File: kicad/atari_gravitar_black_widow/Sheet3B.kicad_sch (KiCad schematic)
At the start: 106 parts, among them Q1 2N3904, Y1 12.096 MHZ

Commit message: C16-30
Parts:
- C18, C19, C20, C21, C22, C25, C26, C37, C40, C41, C42, C43, C45, C46, C47, C48, C49, C50, C51, C52, C53, C54, C55, C56, C57, C58, C59, C60, C61, C62, C63: footprint (none) -> Star_Wars_Vector_PCB:GenericComp
- C23, C24: footprint (none) -> Star_Wars_Vector_PCB:CapBrown
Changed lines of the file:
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@@
       (effects (font (size 1.27 1.27)) (justify left))
     )
-    (property "Footprint" "" (id 2) (at 147.0152 207.01 0)
+    (property "Footprint" "Star_Wars_Vector_PCB:GenericComp" (id 2) (at 147.0152 207.01 0)
       (effects (font (size 1.27 1.27)) hide)
     )
@@
       (effects (font (size 1.27 1.27)) (justify left))
     )
-    (property "Footprint" "" (id 2) (at 108.9152 223.52 0)
+    (property "Footprint" "Star_Wars_Vector_PCB:GenericComp" (id 2) (at 108.9152 223.52 0)
       (effects (font (size 1.27 1.27)) hide)
     )
@@
       (effects (font (size 1.27 1.27)) (justify left))
     )
-    (property "Footprint" "" (id 2) (at 118.4402 223.52 0)
+    (property "Footprint" "Star_Wars_Vector_PCB:GenericComp" (id 2) (at 118.4402 223.52 0)
       (effects (font (size 1.27 1.27)) hide)
     )
@@
       (effects (font (size 1.27 1.27)) (justify left))
     )
-    (property "Footprint" "" (id 2) (at 127.9652 223.52 0)
+    (property "Footprint" "Star_Wars_Vector_PCB:GenericComp" (id 2) (at 127.9652 223.52 0)
       (effects (font (size 1.27 1.27)) hide)
     )
@@
       (effects (font (size 1.27 1.27)) (justify left))
     )
-    (property "Footprint" "" (id 2) (at 137.4902 223.52 0)
+    (property "Footprint" "Star_Wars_Vector_PCB:GenericComp" (id 2) (at 137.4902 223.52 0)
       (effects (font (size 1.27 1.27)) hide)
     )
@@
       (effects (font (size 1.27 1.27)) (justify left))
     )
-    (property "Footprint" "" (id 2) (at 147.0152 223.52 0)
+    (property "Footprint" "Star_Wars_Vector_PCB:GenericComp" (id 2) (at 147.0152 223.52 0)
       (effects (font (size 1.27 1.27)) hide)
     )
@@
       (effects (font (size 1.27 1.27)) (justify left))
     )
-    (property "Footprint" "" (id 2) (at 73.3552 242.57 0)
+    (property "Footprint" "Star_Wars_Vector_PCB:GenericComp" (id 2) (at 73.3552 242.57 0)
       (effects (font (size 1.27 1.27)) hide)
     )
@@
       (effects (font (size 1.27 1.27)) (justify left))
     )
-    (property "Footprint" "" (id 2) (at 82.8802 242.57 0)
+    (property "Footprint" "Star_Wars_Vector_PCB:GenericComp" (id 2) (at 82.8802 242.57 0)
       (effects (font (size 1.27 1.27)) hide)
     )
@@
       (effects (font (size 1.27 1.27)) (justify left))
     )
-    (property "Footprint" "" (id 2) (at 92.4052 242.57 0)
+    (property "Footprint" "Star_Wars_Vector_PCB:GenericComp" (id 2) (at 92.4052 242.57 0)
       (effects (font (size 1.27 1.27)) hide)
     )
@@
       (effects (font (size 1.27 1.27)) (justify left))
     )
-    (property "Footprint" "" (id 2) (at 101.9302 242.57 0)
+    (property "Footprint" "Star_Wars_Vector_PCB:GenericComp" (id 2) (at 101.9302 242.57 0)
       (effects (font (size 1.27 1.27)) hide)
     )
@@
       (effects (font (size 1.27 1.27)) (justify left))
     )
-    (property "Footprint" "" (id 2) (at 111.4552 242.57 0)
+    (property "Footprint" "Star_Wars_Vector_PCB:GenericComp" (id 2) (at 111.4552 242.57 0)
       (effects (font (size 1.27 1.27)) hide)
     )
@@
       (effects (font (size 1.27 1.27)) (justify left))
     )
-    (property "Footprint" "" (id 2) (at 120.9802 242.57 0)
+    (property "Footprint" "Star_Wars_Vector_PCB:GenericComp" (id 2) (at 120.9802 242.57 0)
       (effects (font (size 1.27 1.27)) hide)
     )
@@
       (effects (font (size 1.27 1.27)) (justify left))
     )
-    (property "Footprint" "" (id 2) (at 130.5052 242.57 0)
+    (property "Footprint" "Star_Wars_Vector_PCB:GenericComp" (id 2) (at 130.5052 242.57 0)
       (effects (font (size 1.27 1.27)) hide)
     )
@@
       (effects (font (size 1.27 1.27)) (justify left))
     )
-    (property "Footprint" "" (id 2) (at 140.0302 242.57 0)
+    (property "Footprint" "Star_Wars_Vector_PCB:GenericComp" (id 2) (at 140.0302 242.57 0)
       (effects (font (size 1.27 1.27)) hide)
     )
@@
       (effects (font (size 1.27 1.27)) (justify left))
     )
-    (property "Footprint" "" (id 2) (at 149.5552 242.57 0)
+    (property "Footprint" "Star_Wars_Vector_PCB:GenericComp" (id 2) (at 149.5552 242.57 0)
       (effects (font (size 1.27 1.27)) hide)
     )
@@
       (effects (font (size 1.27 1.27)) (justify left))
     )
-    (property "Footprint" "" (id 2) (at 159.0802 242.57 0)
+    (property "Footprint" "Star_Wars_Vector_PCB:GenericComp" (id 2) (at 159.0802 242.57 0)
       (effects (font (size 1.27 1.27)) hide)
     )
@@
       (effects (font (size 1.27 1.27)) (justify left))
     )
-    (property "Footprint" "" (id 2) (at 73.3552 259.08 0)
+    (property "Footprint" "Star_Wars_Vector_PCB:GenericComp" (id 2) (at 73.3552 259.08 0)
       (effects (font (size 1.27 1.27)) hide)
     )
@@
       (effects (font (size 1.27 1.27)) (justify left))
     )
-    (property "Footprint" "" (id 2) (at 82.8802 259.08 0)
+    (property "Footprint" "Star_Wars_Vector_PCB:GenericComp" (id 2) (at 82.8802 259.08 0)
       (effects (font (size 1.27 1.27)) hide)
     )
@@
       (effects (font (size 1.27 1.27)) (justify left))
     )
-    (property "Footprint" "" (id 2) (at 92.4052 259.08 0)
+    (property "Footprint" "Star_Wars_Vector_PCB:GenericComp" (id 2) (at 92.4052 259.08 0)
       (effects (font (size 1.27 1.27)) hide)
     )
@@
       (effects (font (size 1.27 1.27)) (justify left))
     )
-    (property "Footprint" "" (id 2) (at 101.9302 259.08 0)
+    (property "Footprint" "Star_Wars_Vector_PCB:GenericComp" (id 2) (at 101.9302 259.08 0)
       (effects (font (size 1.27 1.27)) hide)
     )
@@
       (effects (font (size 1.27 1.27)) (justify left))
     )
-    (property "Footprint" "" (id 2) (at 111.4552 259.08 0)
+    (property "Footprint" "Star_Wars_Vector_PCB:GenericComp" (id 2) (at 111.4552 259.08 0)
       (effects (font (size 1.27 1.27)) hide)
     )
@@
       (effects (font (size 1.27 1.27)) (justify left))
     )
-    (property "Footprint" "" (id 2) (at 120.9802 259.08 0)
+    (property "Footprint" "Star_Wars_Vector_PCB:GenericComp" (id 2) (at 120.9802 259.08 0)
       (effects (font (size 1.27 1.27)) hide)
     )
@@
       (effects (font (size 1.27 1.27)) (justify left))
     )
-    (property "Footprint" "" (id 2) (at 130.5052 259.08 0)
+    (property "Footprint" "Star_Wars_Vector_PCB:GenericComp" (id 2) (at 130.5052 259.08 0)
       (effects (font (size 1.27 1.27)) hide)
     )
@@
       (effects (font (size 1.27 1.27)) (justify left))
     )
-    (property "Footprint" "" (id 2) (at 140.0302 259.08 0)
+    (property "Footprint" "Star_Wars_Vector_PCB:GenericComp" (id 2) (at 140.0302 259.08 0)
       (effects (font (size 1.27 1.27)) hide)
     )
@@
       (effects (font (size 1.27 1.27)) (justify left))
     )
-    (property "Footprint" "" (id 2) (at 149.5552 259.08 0)
+    (property "Footprint" "Star_Wars_Vector_PCB:GenericComp" (id 2) (at 149.5552 259.08 0)
       (effects (font (size 1.27 1.27)) hide)
     )
@@
       (effects (font (size 1.27 1.27)) (justify left))
     )
-    (property "Footprint" "" (id 2) (at 159.0802 259.08 0)
+    (property "Footprint" "Star_Wars_Vector_PCB:GenericComp" (id 2) (at 159.0802 259.08 0)
       (effects (font (size 1.27 1.27)) hide)
     )
@@
       (effects (font (size 1.27 1.27)) (justify left))
     )
-    (property "Footprint" "" (id 2) (at 73.3552 275.59 0)
+    (property "Footprint" "Star_Wars_Vector_PCB:GenericComp" (id 2) (at 73.3552 275.59 0)
       (effects (font (size 1.27 1.27)) hide)
     )
@@
       (effects (font (size 1.27 1.27)) (justify left))
     )
-    (property "Footprint" "" (id 2) (at 82.8802 275.59 0)
+    (property "Footprint" "Star_Wars_Vector_PCB:GenericComp" (id 2) (at 82.8802 275.59 0)
       (effects (font (size 1.27 1.27)) hide)
     )
@@
       (effects (font (size 1.27 1.27)) (justify left))
     )
-    (property "Footprint" "" (id 2) (at 92.4052 275.59 0)
+    (property "Footprint" "Star_Wars_Vector_PCB:GenericComp" (id 2) (at 92.4052 275.59 0)
       (effects (font (size 1.27 1.27)) hide)
     )
@@
       (effects (font (size 1.27 1.27)) (justify left))
     )
-    (property "Footprint" "" (id 2) (at 277.8252 153.67 0)
+    (property "Footprint" "Star_Wars_Vector_PCB:CapBrown" (id 2) (at 277.8252 153.67 0)
       (effects (font (size 1.27 1.27)) hide)
     )
@@
       (effects (font (size 1.27 1.27)) (justify left))
     )
-    (property "Footprint" "" (id 2) (at 277.8252 165.735 0)
+    (property "Footprint" "Star_Wars_Vector_PCB:CapBrown" (id 2) (at 277.8252 165.735 0)
       (effects (font (size 1.27 1.27)) hide)
     )
@@
     (property "Reference" "C22" (id 0) (at 286.385 129.4892 90))
     (property "Value" ".1uf" (id 1) (at 286.385 131.8006 90))
-    (property "Footprint" "" (id 2) (at 282.575 136.8552 0)
+    (property "Footprint" "Star_Wars_Vector_PCB:GenericComp" (id 2) (at 282.575 136.8552 0)
       (effects (font (size 1.27 1.27)) hide)
     )
@@
       (effects (font (size 1.27 1.27)) (justify left))
     )
-    (property "Footprint" "" (id 2) (at 279.4 211.1502 0)
-      (effects (font (size 1.27 1.27)) hide)
-    )
+    (property "Footprint" "Star_Wars_Vector_PCB:GenericComp" (id 2) (at 279.4 211.1502 0)
+      (effects (font (size 1.27 1.27)) hide)
+    )

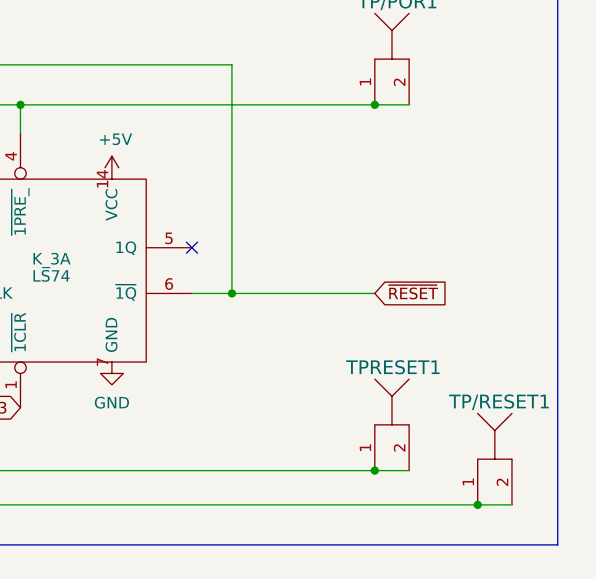
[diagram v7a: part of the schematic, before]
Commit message: Added traces and bottom image
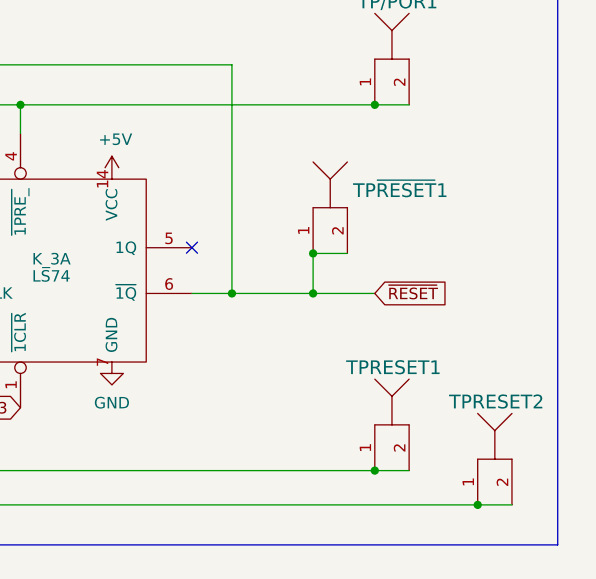
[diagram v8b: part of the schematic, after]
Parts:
- added TP~{RESET}1: TP, quantum_arcade_pcb:TP, symbol atari_grav_bw:TP
- renumbered TP/RESET1 to TPRESET2
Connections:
- net ~{RESET}: now also TP~{RESET}1.1, TP~{RESET}1.2
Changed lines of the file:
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@@
   (junction (at 117.475 208.28) (diameter 0) (color 0 0 0 0)
   )
+  (junction (at 498.602 266.7) (diameter 0) (color 0 0 0 0)
+  )
   (junction (at 111.125 133.985) (diameter 0) (color 0 0 0 0)
   )
@@
   (junction (at 306.705 153.67) (diameter 0) (color 0 0 0 0)
   )
+  (junction (at 498.602 262.255) (diameter 0) (color 0 0 0 0)
+  )
   (junction (at 129.54 243.84) (diameter 0) (color 0 0 0 0)
   )
@@
     (stroke (width 0) (type default) (color 0 0 0 0))
   )
-  (wire (pts (xy 489.585 266.7) (xy 505.46 266.7))
+  (wire (pts (xy 489.585 266.7) (xy 498.602 266.7))
     (stroke (width 0) (type default) (color 0 0 0 0))
   )
@@
     (stroke (width 0) (type default) (color 0 0 0 0))
   )
+  (wire (pts (xy 498.602 262.255) (xy 498.602 266.7))
+    (stroke (width 0) (type default) (color 0 0 0 0))
+  )
   (wire (pts (xy 318.135 153.67) (xy 306.705 153.67))
     (stroke (width 0) (type default) (color 0 0 0 0))
@@
     (stroke (width 0) (type default) (color 0 0 0 0))
   )
+  (wire (pts (xy 498.602 262.255) (xy 502.412 262.255))
+    (stroke (width 0) (type default) (color 0 0 0 0))
+  )
   (wire (pts (xy 372.745 187.96) (xy 359.41 187.96))
     (stroke (width 0) (type default) (color 0 0 0 0))
@@
     (stroke (width 0) (type default) (color 0 0 0 0))
   )
+  (wire (pts (xy 498.602 266.7) (xy 505.46 266.7))
+    (stroke (width 0) (type default) (color 0 0 0 0))
+  )
   (text "Power-On Reset" (at 300.99 192.405 0)
     (effects (font (size 2.54 2.54) (thickness 0.508) bold) (justify left bottom))
@@
   (symbol (lib_id "atari_grav_bw:TP") (at 518.795 285.115 0) (unit 1)
     (in_bom yes) (on_board yes)
-    (property "Reference" "TP/RESET1" (id 0) (at 513.715 278.765 0)
+    (property "Reference" "TPRESET2" (id 0) (at 513.715 278.765 0)
       (effects (font (size 1.524 1.524)) (justify left))
     )
@@
     (pin "1")
   )
+  (symbol (lib_id "atari_grav_bw:TP") (at 500.507 257.175 0) (unit 1)
+    (in_bom yes) (on_board yes) (fields_autoplaced)
+    (property "Reference" "TP~{RESET}1" (id 0) (at 503.047 255.28 0)
+      (effects (font (size 1.524 1.524)) (justify left))
+    )
+    (property "Value" "TP" (id 1) (at 498.602 255.905 0)
+      (effects (font (size 1.524 1.524)) hide)
+    )
+    (property "Footprint" "quantum_arcade_pcb:TP" (id 2) (at 498.602 258.445 0)
+      (effects (font (size 1.524 1.524)) hide)
+    )
+    (property "Datasheet" "" (id 3) (at 498.602 258.445 0)
+      (effects (font (size 1.524 1.524)) hide)
+    )
+    (pin "1")
+    (pin "2")
+  )
   (symbol (lib_id "power:+10V") (at 274.955 225.425 180) (unit 1)
